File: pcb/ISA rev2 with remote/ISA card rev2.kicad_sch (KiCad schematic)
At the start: 28 parts, among them J1 PCB_Finger_ISA_8bit, J2 OLED Header, J3 remote header, J4 OLED here, J5 Button Header, SW1 Up, SW2 Down, SW3 Select/Menu, U1 74LVC02, U2 74LVC245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

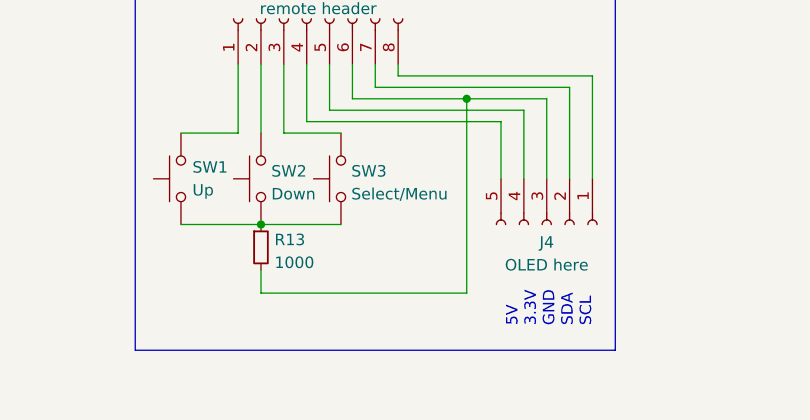
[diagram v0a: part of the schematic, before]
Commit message: more available 74LVC02 footprint; generate gbrs
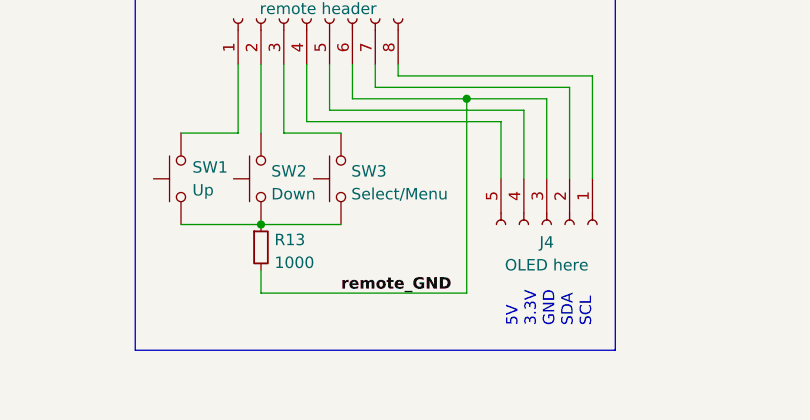
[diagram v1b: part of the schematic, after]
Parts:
- U1: footprint Package_SO:SO-14_5.3x10.2mm_P1.27mm -> Package_SO:SO-14_3.9x8.65mm_P1.27mm
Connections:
- net remote_GND: now reaches J3.6 (Pin_6), J4.3 (Pin_3), R13.2
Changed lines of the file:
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@@
     (effects (font (size 1.27 1.27)) (justify left bottom))
+  )
+  (label "remote_GND" (at 99.06 182.88 0)
+    (effects (font (size 1.27 1.27) bold) (justify left bottom))
   )
   (label "-5Vmon" (at 53.34 124.46 0)
@@
     (property "Reference" "U1" (id 0) (at 62.23 104.14 0))
     (property "Value" "74LVC02" (id 1) (at 62.23 106.68 0))
-    (property "Footprint" "Package_SO:SO-14_5.3x10.2mm_P1.27mm" (id 2) (at 63.5 111.76 0)
+    (property "Footprint" "Package_SO:SO-14_3.9x8.65mm_P1.27mm" (id 2) (at 63.5 111.76 0)
       (effects (font (size 1.27 1.27)) hide)
     )
@@
       (effects (font (size 1.27 1.27)) (justify left))
     )
-    (property "Footprint" "Package_SO:SO-14_5.3x10.2mm_P1.27mm" (id 2) (at 21.59 176.53 0)
+    (property "Footprint" "Package_SO:SO-14_3.9x8.65mm_P1.27mm" (id 2) (at 21.59 176.53 0)
       (effects (font (size 1.27 1.27)) hide)
     )
@@
     (property "Reference" "U1" (id 0) (at 180.34 57.2602 0))
     (property "Value" "74LVC02" (id 1) (at 180.34 59.7971 0))
-    (property "Footprint" "Package_SO:SO-14_5.3x10.2mm_P1.27mm" (id 2) (at 180.34 64.77 0)
+    (property "Footprint" "Package_SO:SO-14_3.9x8.65mm_P1.27mm" (id 2) (at 180.34 64.77 0)
       (effects (font (size 1.27 1.27)) hide)
     )
@@
     )
     (path "/1686cfbf-ef14-447b-b680-0abc1f742d3f"
-      (reference "U1") (unit 1) (value "74LVC02") (footprint "Package_SO:SO-14_5.3x10.2mm_P1.27mm")
+      (reference "U1") (unit 1) (value "74LVC02") (footprint "Package_SO:SO-14_3.9x8.65mm_P1.27mm")
     )
     (path "/e381a004-7785-4beb-9895-0343374a3f2f"
-      (reference "U1") (unit 2) (value "74LVC02") (footprint "Package_SO:SO-14_5.3x10.2mm_P1.27mm")
+      (reference "U1") (unit 2) (value "74LVC02") (footprint "Package_SO:SO-14_3.9x8.65mm_P1.27mm")
     )
     (path "/9fe563c8-7eb9-4be8-8f3c-bfd764c64f9b"
-      (reference "U1") (unit 5) (value "74LVC02") (footprint "Package_SO:SO-14_5.3x10.2mm_P1.27mm")
+      (reference "U1") (unit 5) (value "74LVC02") (footprint "Package_SO:SO-14_3.9x8.65mm_P1.27mm")
     )
     (path "/bc0acec4-eee5-49e7-9990-2a24d7bb37e6"
